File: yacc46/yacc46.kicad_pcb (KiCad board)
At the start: 2 copper layers, 281.1 x 112.1 mm, 142 parts, among them J1 CX70M-24P1, J2 OLED_I2C, J3 AVR-ISP-6, J4 GLOVE_I2C, J5 TRRS_I2C, SW1 SW_PUSH, SW10 SW_PUSH, SW11 SW_PUSH, SW12 SW_PUSH, SW13 SW_PUSH, SW14 SW_PUSH, SW15 SW_PUSH, SW16 SW_PUSH, SW17 SW_PUSH, SW18 SW_PUSH, SW19 Rotary_Encoder_Switch, SW2 SW_PUSH, SW20 SW_PUSH, SW21 SW_PUSH, SW22 SW_PUSH, SW23 SW_PUSH, SW24 SW_PUSH, SW25 SW_PUSH, SW26 SW_PUSH, SW27 SW_PUSH, SW28 SW_PUSH, SW29 SW_PUSH, SW3 SW_PUSH, SW30 SW_PUSH, SW31 SW_PUSH, SW32 SW_PUSH, SW33 SW_PUSH, SW34 SW_PUSH, SW35 SW_PUSH, SW36 Rotary_Encoder_Switch, SW37 SW_PUSH, SW38 SW_PUSH, SW39 SW_PUSH, SW4 SW_PUSH, SW40 SW_PUSH, SW41 SW_PUSH, SW42 SW_PUSH, SW43 SW_PUSH, SW44 SW_PUSH, SW45 SW_PUSH, SW46 SW_PUSH, SW47 SW_Push, SW5 SW_PUSH, SW6 SW_PUSH, SW7 SW_PUSH, SW8 SW_PUSH, SW9 SW_PUSH, U1 ATmega32U4-AU, Y1 16MHz

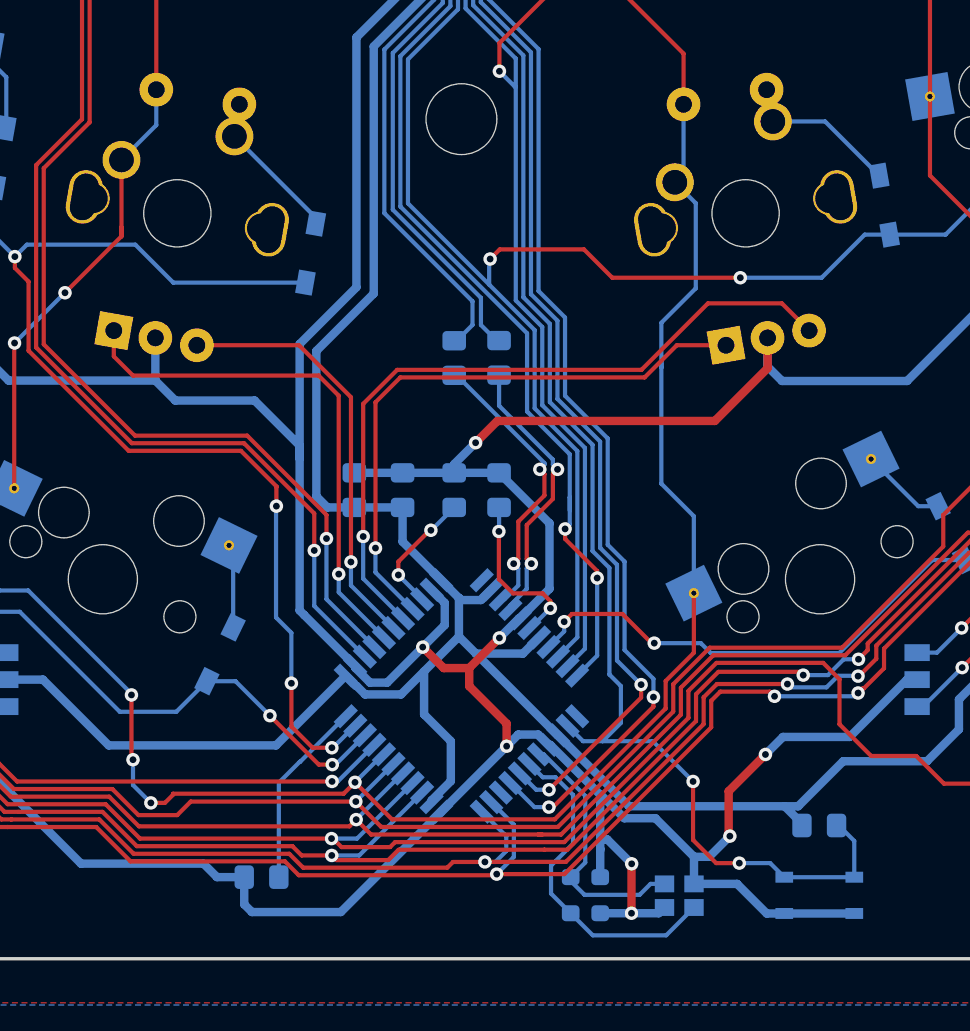
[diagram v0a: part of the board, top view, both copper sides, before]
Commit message: ロータリーエンコーダ部分のスイッチをMillMaxソケットに対応
スイッチ用スルーホールを直径1.6mmに変更
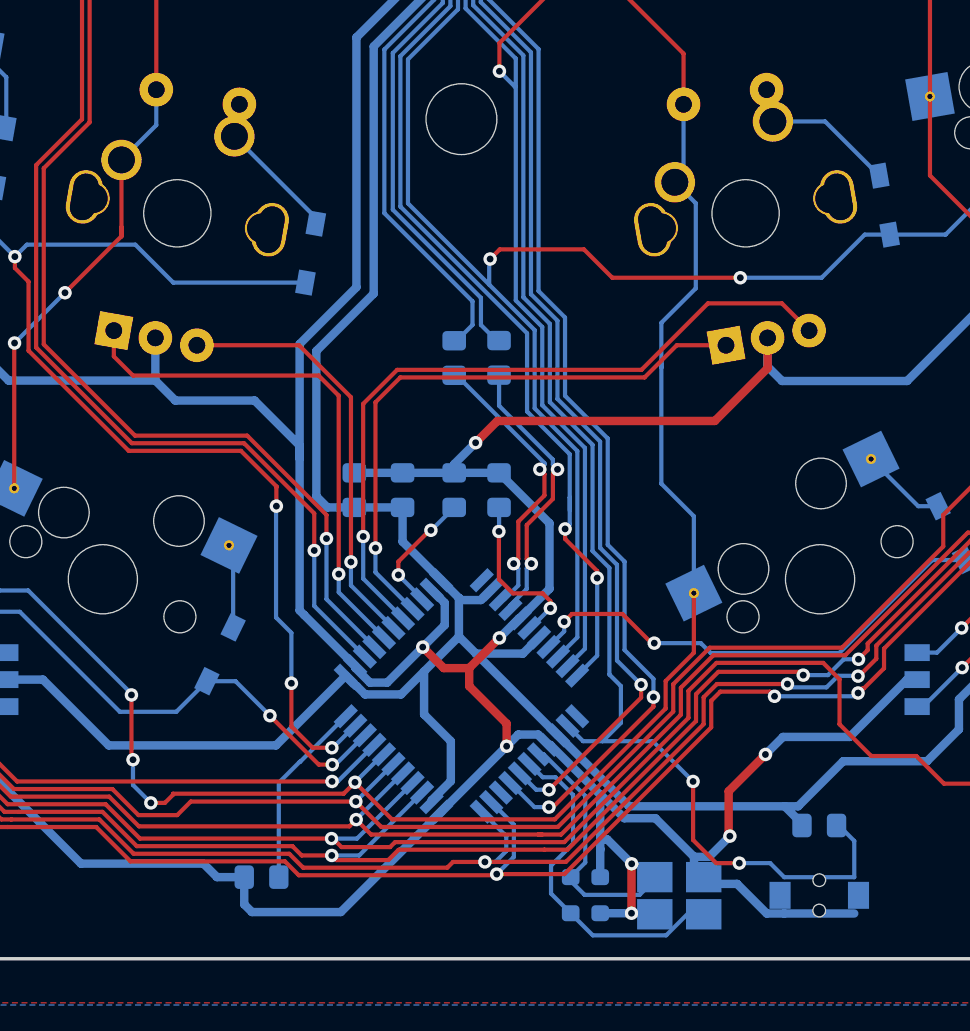
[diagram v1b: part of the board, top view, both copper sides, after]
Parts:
- SW47: footprint 1m38_kbd:ResetSW_SKRPABE010 -> 1m38_kbd:SW_PUSH_SMD_TVAF06-A020B-R_HandSolder
- Y1: footprint Crystal:Crystal_SMD_2520-4Pin_2.5x2.0mm -> Crystal:Crystal_SMD_SeikoEpson_FA238-4Pin_3.2x2.5mm_HandSoldering

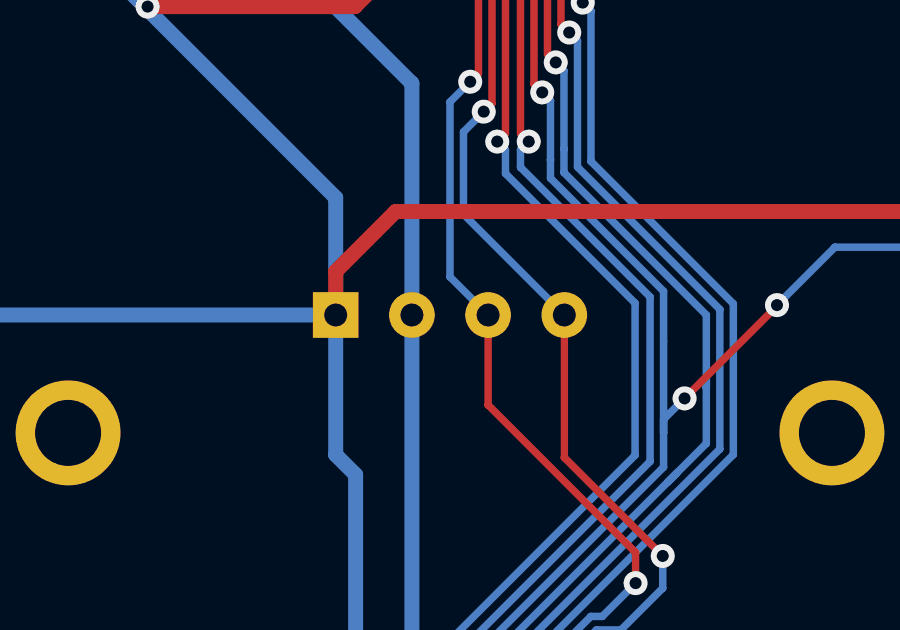
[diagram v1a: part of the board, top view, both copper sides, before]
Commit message: OLEDのフットプリントを修正
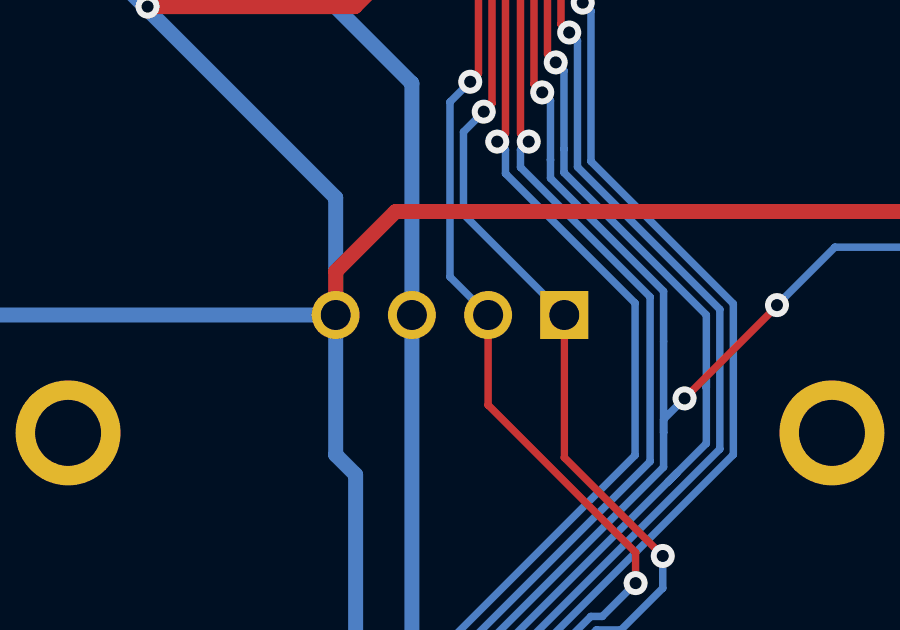
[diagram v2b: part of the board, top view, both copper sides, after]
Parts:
- turned J2 to 180 degrees

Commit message: 配線を修正
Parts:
- moved D35 4.98 mm to (302.5, 71.6)
- moved D42 4.98 mm to (302.5, 90.6)
- moved D41 3.06 mm to (286.5, 88.1)
- moved C5 2.26 mm to (172.1, 133.0)
- moved C6 2.13 mm to (172.1, 135.2)
- turned SW47 to 180 degrees
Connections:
- U1 pad 16: XTAL2 -> XTAL1
- U1 pad 17: XTAL1 -> XTAL2
- Y1 pad 1: XTAL1 -> XTAL2
- Y1 pad 3: XTAL2 -> XTAL1
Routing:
- net VBUS: track 857.1 -> 850.0 mm, vias 0 -> 1
- net ROWR2: track 321.8 -> 315.7 mm, vias 7 -> 5
- net XTAL2: track 15.8 -> 21.8 mm
- net Net-(D42-Pad2): track 5.23 -> 10.2 mm
- net Net-(D35-Pad2): track 5.23 -> 10.2 mm
- net ROWL2: track 183.8 -> 179.0 mm
- net XTAL1: track 19.9 -> 16.2 mm
- net MOSI: track 312.9 -> 309.2 mm, vias 7 -> 5
- net UDN: track 236.8 -> 233.3 mm, vias 4 -> 2
- net UDP: track 240.1 -> 236.6 mm, vias 4 -> 2
- net RESET: track 170.5 -> 168.1 mm, vias 3 -> 5
- net Net-(LED3-Pad3): track 97.7 -> 95.4 mm
- net COL1: track 368.7 -> 366.3 mm, vias 8 -> 7
- net Net-(LED2-Pad3): track 88.4 -> 90.7 mm
- net SDA: track 268.4 -> 270.6 mm, vias 6 -> 5
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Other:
- board text added: "RESET"
- board text added: "yacc46 v0.2 PCB designed by 1.038"
- board text removed: "yacc46 v0.1 PCB designed by 1.038"

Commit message: key_arrange.pyを変更、フットプリントの位置を微調整
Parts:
- removed the HOLE13 at (152.0, 60.1)
- removed the HOLE13 at (164.8, 88.2)
- removed J5: TRRS_I2C, 1m38_kbd:MJ-4PP-9_1side_no-mask
- added HOLE13: Val**, foostan_kbd:M2_HOLE_v2, F.Cu at (165.0, 88.2)
- added HOLE15: MountingHole_2.2mm_M2, MountingHole:MountingHole_2.2mm_M2, F.Cu at (178.0, 60.1)
- C1, C2, C3, C4: footprint Capacitor_SMD:C_0805_2012Metric_Pad1.15x1.40mm_HandSolder -> Capacitor_SMD:C_0805_2012Metric_Pad1.18x1.45mm_HandSolder
- C5, C6: footprint Capacitor_SMD:C_0603_1608Metric_Pad1.05x0.95mm_HandSolder -> Capacitor_SMD:C_0603_1608Metric_Pad1.08x0.95mm_HandSolder
- HOLE1, HOLE10, HOLE11, HOLE12, HOLE2, HOLE3, HOLE4, HOLE5, HOLE6, HOLE7, HOLE8, HOLE9: footprint foostan-kbd:M2_HOLE_v2 -> foostan_kbd:M2_HOLE_v2
- R1, R2, R3, R4, R5, R6: footprint Resistor_SMD:R_0805_2012Metric_Pad1.15x1.40mm_HandSolder -> Resistor_SMD:R_0805_2012Metric_Pad1.20x1.40mm_HandSolder
- moved J4 367.7 mm to (49.1, 320.5), turned to 0 degrees
- moved F1 340.9 mm to (85.4, 378.0)
- moved J3 337.9 mm to (46.1, 358.3), turned to 180 degrees
- moved R1 337.3 mm to (91.8, 383.1)
- moved R2 321.2 mm to (79.2, 371.1), turned to 180 degrees
- moved R5 287.7 mm to (59.3, 388.4), turned to 180 degrees
- moved R3 279.7 mm to (116.5, 377.9), turned to 180 degrees
- moved U1 272.8 mm to (36.6, 363.2), turned to 180 degrees
- moved R4 266.2 mm to (154.9, 368.3), turned to 180 degrees
- moved C4 264.8 mm to (163.2, 374.9), turned to 180 degrees
- moved C1 260.5 mm to (102.8, 364.7), turned to 180 degrees
- moved C3 258.1 mm to (127.8, 365.7), turned to 180 degrees
- moved C2 254.3 mm to (153.0, 364.4), turned to 180 degrees
- moved Y1 253.0 mm to (59.0, 357.6)
- moved R6 243.1 mm to (111.3, 372.6), turned to 180 degrees
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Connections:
- U1 pad 16: XTAL1 -> XTAL2
- U1 pad 17: XTAL2 -> XTAL1
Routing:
- net GND: track 946.6 -> 0.00 mm, vias 15 -> 0
- net VBUS: track 850.0 -> 0.00 mm, vias 1 -> 0
- net COL0: track 367.2 -> 0.00 mm, vias 6 -> 0
- net COL1: track 366.3 -> 0.00 mm, vias 7 -> 0
- net COL2: track 342.7 -> 0.00 mm, vias 9 -> 0
- net COL3: track 341.0 -> 0.00 mm, vias 7 -> 0
- net ROWR2: track 315.7 -> 0.00 mm, vias 5 -> 0
- net MOSI: track 309.2 -> 0.00 mm, vias 5 -> 0
- net MISO: track 300.1 -> 0.00 mm, vias 9 -> 0
- net COL4: track 292.4 -> 0.00 mm, vias 6 -> 0
- net SDA: track 270.6 -> 0.00 mm, vias 5 -> 0
- net SCL: track 265.1 -> 0.00 mm, vias 6 -> 0
- net COL5: track 240.2 -> 0.00 mm, vias 5 -> 0
- net UDP: track 236.6 -> 0.00 mm, vias 2 -> 0
- net UDN: track 233.3 -> 0.00 mm, vias 2 -> 0
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- removed copper zone on B.Cu, net GND
- removed copper zone on F.Cu, net GND
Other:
- board outline removed
- board text removed: "RESET"
- board text removed: "yacc46 v0.2 PCB designed by 1.038"

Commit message: 基板外形を変更
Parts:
- moved F1 341.6 mm to (50.2, 38.1)
- moved J3 338.5 mm to (118.6, 27.7), turned to 270 degrees
- moved R1 334.8 mm to (40.0, 52.2)
- moved J4 326.4 mm to (205.6, 34.1), turned to 270 degrees
- moved R2 323.9 mm to (40.0, 49.7), turned to 0 degrees
- moved U1 282.8 mm to (165.0, 111.2), turned to 225 degrees
- moved R5 270.5 mm to (178.1, 145.4)
- moved Y1 255.4 mm to (164.9, 125.2)
- moved C6 240.1 mm to (169.7, 125.2), turned to 90 degrees
- moved C5 238.4 mm to (160.3, 125.3), turned to 270 degrees
- moved R3 229.4 mm to (182.2, 158.1)
- moved C1 229.4 mm to (168.5, 144.9)
- moved C3 229.4 mm to (193.5, 145.9)
- moved R6 229.4 mm to (176.9, 152.8)
- moved J2 229.0 mm to (165.0, 56.7)
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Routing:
- net GND: track 0.00 -> 29.5 mm
- net XTAL1: track 0.00 -> 19.2 mm
- net XTAL2: track 0.00 -> 16.3 mm
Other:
- board outline added: 281.5 x 112.1 mm

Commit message: 配線完了
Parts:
- moved C4 75.7 mm to (168.1, 96.7), turned to 90 degrees
- moved R4 72.2 mm to (168.1, 90.1), turned to 270 degrees
- moved R3 70.0 mm to (165.6, 90.1), turned to 90 degrees
- moved C2 63.8 mm to (163.3, 96.7), turned to 270 degrees
- moved C3 56.6 mm to (165.7, 96.7), turned to 90 degrees
- moved C1 48.8 mm to (161.0, 96.7), turned to 270 degrees
- moved SW47 42.5 mm to (184.1, 132.6), turned to 0 degrees
- moved R6 31.2 mm to (153.2, 132.6), turned to 0 degrees
- moved R5 12.8 mm to (177.5, 132.6), turned to 0 degrees
- moved HOLE13 8.09 mm to (165.0, 80.1)
- moved Y1 7.07 mm to (172.0, 125.7)
- moved C6 7.01 mm to (176.6, 125.7)
- moved C5 7.00 mm to (167.3, 125.7)
- moved D35 5.49 mm to (302.4, 71.9)
- moved D42 5.49 mm to (302.4, 90.9)
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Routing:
- net VBUS: track 0.00 -> 777.4 mm
- net COL0: track 0.00 -> 386.3 mm, vias 0 -> 5
- net COL1: track 0.00 -> 382.3 mm, vias 0 -> 10
- net COL2: track 0.00 -> 365.1 mm, vias 0 -> 7
- net COL3: track 0.00 -> 356.6 mm, vias 0 -> 5
- net COL4: track 0.00 -> 300.7 mm, vias 0 -> 6
- net MOSI: track 0.00 -> 292.5 mm, vias 0 -> 5
- net ROWR2: track 0.00 -> 292.4 mm, vias 0 -> 4
- net MISO: track 0.00 -> 287.1 mm, vias 0 -> 9
- net COL5: track 0.00 -> 265.7 mm, vias 0 -> 5
- net UDN: track 0.00 -> 213.3 mm, vias 0 -> 2
- net UDP: track 0.00 -> 210.6 mm, vias 0 -> 2
- net COL6: track 0.00 -> 184.9 mm, vias 0 -> 3
- net ROWL1: track 0.00 -> 166.9 mm, vias 0 -> 4
- net RESET: track 0.00 -> 163.4 mm, vias 0 -> 4
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- added copper zone on B.Cu, net GND
- added copper zone on F.Cu, net GND
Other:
- board text added: "RST"

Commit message: GND配線を修正
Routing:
- net GND: track 131.7 -> 909.4 mm, vias 18 -> 59
- net ENCR2: track 32.7 -> 35.0 mm
- net Net-(LED6-Pad3): track 112.9 -> 110.7 mm
- net VBUS: track 777.4 -> 775.5 mm
- net ROWL2: track 156.4 -> 158.0 mm
- net RESET: track 163.4 -> 164.2 mm
- net MISO: track 287.1 -> 287.8 mm
- net SCL: track 123.6 -> 124.2 mm
- net SDA: track 124.3 -> 124.9 mm
- net Net-(LED10-Pad3): track 61.1 -> 61.6 mm
- net COL1: vias 10 -> 9

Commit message: クレジットを追加
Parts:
- moved R6 2.19 mm to (152.3, 130.6)
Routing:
- net GND: track 909.4 -> 898.8 mm, vias 59 -> 58
- net HWB: track 21.8 -> 20.2 mm
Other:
- board text added: "yacc46 v0.2 PCB designed by 1.038"
